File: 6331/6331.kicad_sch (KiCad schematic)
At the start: 2 parts, among them U1 ATF22V10C-10PU

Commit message: PCB update to fix power trace widths and add board rev
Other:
- title: (none) -> 22V10 to 6331 biPROM
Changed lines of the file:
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@@
 	(generator "eeschema")
 	(generator_version "8.0")
-	(paper "A4")
+	(paper "A")
+	(title_block
+		(title "22V10 to 6331 biPROM")
+		(date "2024-08-03")
+		(rev "1.0")
+	)
 	(wire
 		(pts

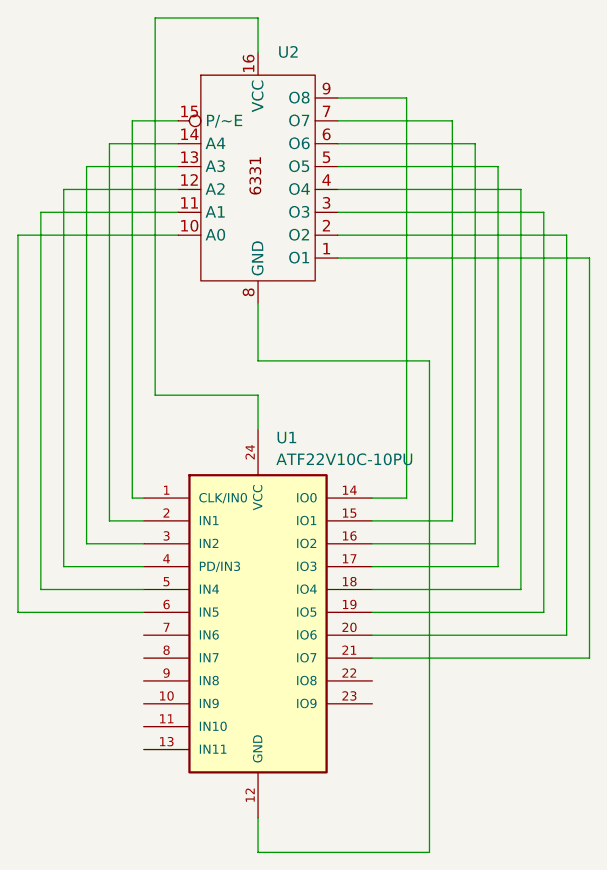
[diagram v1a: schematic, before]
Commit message: Better layout of PCB to simplify construction.  V1.2 of design.
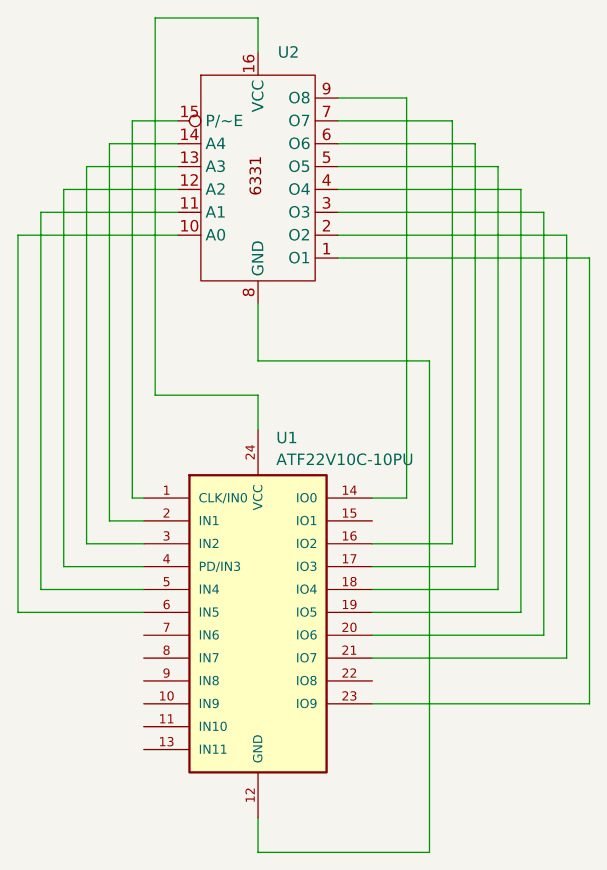
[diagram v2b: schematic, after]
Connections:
- net at U2.1 (O1): now also U1.23 (IO9); no longer U1.21 (IO7)
- net at U2.2 (O2): now also U1.21 (IO7); no longer U1.20 (IO6)
- net at U2.3 (O3): now also U1.20 (IO6); no longer U1.19 (IO5)
- net at U2.4 (O4): now also U1.19 (IO5); no longer U1.18 (IO4)
- net at U2.5 (O5): now also U1.18 (IO4); no longer U1.17 (IO3)
- net at U2.6 (O6): now also U1.17 (IO3); no longer U1.16 (IO2)
- net at U2.7 (O7): now also U1.16 (IO2); no longer U1.15 (IO1)
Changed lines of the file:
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@@
 		(title "22V10 to 6331 biPROM")
 		(date "2024-08-03")
-		(rev "1.0")
-	)
-	(wire
-		(pts
-			(xy 170.18 102.87) (xy 161.29 102.87)
-		)
-		(stroke
-			(width 0)
-			(type default)
-		)
-	)
-	(wire
-		(pts
-			(xy 180.34 68.58) (xy 180.34 113.03)
+		(rev "1.2")
+	)
+	(wire
+		(pts
+			(xy 180.34 68.58) (xy 180.34 115.57)
 		)
 		(stroke
@@
 	(wire
 		(pts
-			(xy 175.26 63.5) (xy 175.26 107.95)
-		)
-		(stroke
-			(width 0)
-			(type default)
-		)
-	)
-	(wire
-		(pts
-			(xy 161.29 118.11) (xy 185.42 118.11)
-		)
-		(stroke
-			(width 0)
-			(type default)
-		)
-	)
-	(wire
-		(pts
 			(xy 121.92 71.12) (xy 121.92 113.03)
 		)
@@
 	(wire
 		(pts
+			(xy 172.72 60.96) (xy 172.72 107.95)
+		)
+		(stroke
+			(width 0)
+			(type default)
+		)
+	)
+	(wire
+		(pts
+			(xy 170.18 105.41) (xy 161.29 105.41)
+		)
+		(stroke
+			(width 0)
+			(type default)
+		)
+	)
+	(wire
+		(pts
+			(xy 161.29 115.57) (xy 180.34 115.57)
+		)
+		(stroke
+			(width 0)
+			(type default)
+		)
+	)
+	(wire
+		(pts
 			(xy 167.64 139.7) (xy 148.59 139.7)
 		)
@@
 	(wire
 		(pts
+			(xy 185.42 123.19) (xy 161.29 123.19)
+		)
+		(stroke
+			(width 0)
+			(type default)
+		)
+	)
+	(wire
+		(pts
 			(xy 175.26 63.5) (xy 157.48 63.5)
 		)
@@
 	(wire
 		(pts
+			(xy 172.72 107.95) (xy 161.29 107.95)
+		)
+		(stroke
+			(width 0)
+			(type default)
+		)
+	)
+	(wire
+		(pts
+			(xy 170.18 58.42) (xy 170.18 105.41)
+		)
+		(stroke
+			(width 0)
+			(type default)
+		)
+	)
+	(wire
+		(pts
 			(xy 134.62 58.42) (xy 134.62 100.33)
 		)
@@
 	(wire
 		(pts
-			(xy 161.29 115.57) (xy 182.88 115.57)
-		)
-		(stroke
-			(width 0)
-			(type default)
-		)
-	)
-	(wire
-		(pts
 			(xy 170.18 58.42) (xy 157.48 58.42)
 		)
@@
 	(wire
 		(pts
+			(xy 177.8 113.03) (xy 161.29 113.03)
+		)
+		(stroke
+			(width 0)
+			(type default)
+		)
+	)
+	(wire
+		(pts
+			(xy 182.88 118.11) (xy 161.29 118.11)
+		)
+		(stroke
+			(width 0)
+			(type default)
+		)
+	)
+	(wire
+		(pts
 			(xy 157.48 71.12) (xy 182.88 71.12)
 		)
@@
 	(wire
 		(pts
-			(xy 170.18 58.42) (xy 170.18 102.87)
-		)
-		(stroke
-			(width 0)
-			(type default)
-		)
-	)
-	(wire
-		(pts
 			(xy 148.59 88.9) (xy 148.59 92.71)
 		)
@@
 	(wire
 		(pts
+			(xy 175.26 63.5) (xy 175.26 110.49)
+		)
+		(stroke
+			(width 0)
+			(type default)
+		)
+	)
+	(wire
+		(pts
 			(xy 167.64 85.09) (xy 167.64 139.7)
 		)
@@
 	(wire
 		(pts
-			(xy 172.72 105.41) (xy 161.29 105.41)
-		)
-		(stroke
-			(width 0)
-			(type default)
-		)
-	)
-	(wire
-		(pts
 			(xy 127 66.04) (xy 127 107.95)
 		)
@@
 	(wire
 		(pts
-			(xy 177.8 66.04) (xy 177.8 110.49)
+			(xy 177.8 66.04) (xy 177.8 113.03)
 		)
 		(stroke
@@
 	(wire
 		(pts
-			(xy 175.26 107.95) (xy 161.29 107.95)
-		)
-		(stroke
-			(width 0)
-			(type default)
-		)
-	)
-	(wire
-		(pts
 			(xy 132.08 60.96) (xy 132.08 102.87)
 		)
@@
 	(wire
 		(pts
+			(xy 161.29 100.33) (xy 165.1 100.33)
+		)
+		(stroke
+			(width 0)
+			(type default)
+		)
+	)
+	(wire
+		(pts
 			(xy 157.48 66.04) (xy 177.8 66.04)
 		)
@@
 	(wire
 		(pts
+			(xy 175.26 110.49) (xy 161.29 110.49)
+		)
+		(stroke
+			(width 0)
+			(type default)
+		)
+	)
+	(wire
+		(pts
 			(xy 129.54 63.5) (xy 129.54 105.41)
 		)
@@
 	(wire
 		(pts
-			(xy 182.88 71.12) (xy 182.88 115.57)
+			(xy 182.88 71.12) (xy 182.88 118.11)
 		)
 		(stroke
@@
 	(wire
 		(pts
-			(xy 185.42 73.66) (xy 185.42 118.11)
-		)
-		(stroke
-			(width 0)
-			(type default)
-		)
-	)
-	(wire
-		(pts
-			(xy 172.72 60.96) (xy 172.72 105.41)
+			(xy 185.42 73.66) (xy 185.42 123.19)
 		)
 		(stroke
@@
 	(wire
 		(pts
-			(xy 161.29 113.03) (xy 180.34 113.03)
-		)
-		(stroke
-			(width 0)
-			(type default)
-		)
-	)
-	(wire
-		(pts
 			(xy 121.92 113.03) (xy 135.89 113.03)
 		)
@@
 	(wire
 		(pts
-			(xy 165.1 100.33) (xy 161.29 100.33)
-		)
-		(stroke
-			(width 0)
-			(type default)
-		)
-	)
-	(wire
-		(pts
 			(xy 148.59 46.99) (xy 137.16 46.99)
 		)
 		(stroke
-			(width 0)
-			(type default)
-		)
-	)
-	(wire
-		(pts
-			(xy 161.29 110.49) (xy 177.8 110.49)
-		)
-		(stroke
